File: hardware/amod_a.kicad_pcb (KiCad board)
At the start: 4 copper layers, 100 x 100 mm, 189 parts, among them J1001 SMA, J1002 SMA, J1003 SMA, J1004 SMA, J101 USB-C, J102 rails, J1101 SMA, J1102 TX, J1103 RX, J1104 Pmod, J1201 SMA, J1202 SMA, J1203 SPK, J1204 MIC, J201 SMA, J202 SMA, J301 SMA, J302 SMA, J401 SMA, J402 SMA, J501 SMA, J502 HB100, J601 SMA, J701 SMA, J702 SMA, J801 SMA, J901 SMA, J902 SMA, J903 SMA, Q1001 AO3401A, Q1101 AO3401A, Q1201 AO3401A, Q201 AO3401A, Q301 AO3401A, Q401 AO3401A, Q501 AO3401A, Q601 AO3401A, Q701 AO3401A, Q801 AO3401A, Q802 AO3400A, Q901 AO3401A, SW1001 ON, SW1002 DIP4, SW1101 ON, SW1201 ON, SW201 ON, SW301 ON, SW401 ON, SW501 ON, SW601 ON, SW701 ON, SW801 ON, SW901 ON, U1001 OPA810, U1002 OPA810, U101 LM2664, U102 3.3V, U1101 DRV8837, U1102 OPA810, U1201 PAM8302A, U1202 OPA810, U201 OPA810, U301 OPA810, U401 OPA847, U501 OPA810, U601 TLV3501, U701 74HC4046A, U801 TMP235, U901 MC1496

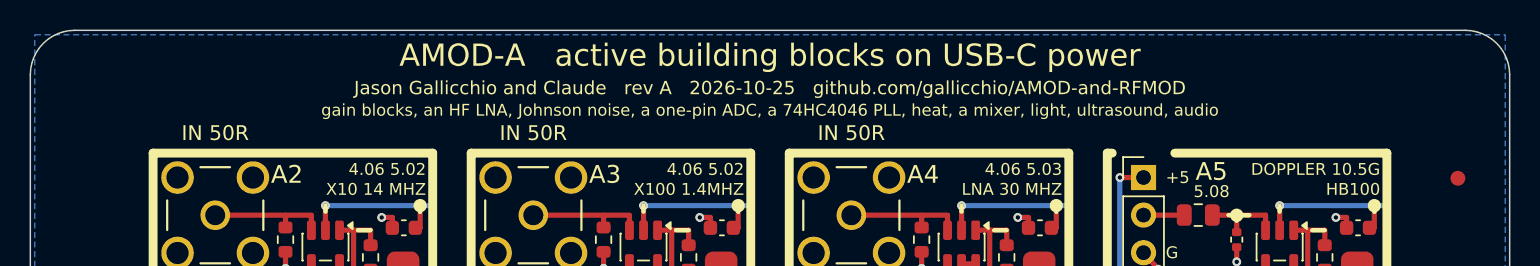
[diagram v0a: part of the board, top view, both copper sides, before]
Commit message: RF-MOD-2 rev A: the coherent I/Q transceiver board (Prompt 13)
Eleven tiles for the ECP5-2ADC-2DAC board: an ADL5375-05 modulator fed by its
DACs (X1), an ADL5380 demodulator with two OPA810 difference amplifiers into its
ADCs (X2), RF-MOD's MAX2871 synthesizer with its own REF IN (X3) split by a
resistive splitter into both LOs (X5), the QPL9547 LNA (X4), an AD8318 log
detector (X6), a switched avalanche noise source with an ADL5611 and a 20 dB
pad (X7), a GNSS front end (bias-T, SAW, MAX2659, SAW: X8), a loop for NV
centres' ODMR with every plane cleared under it (X9), USB-C and -5 V (X10) and
a SKY13370 absorptive SPDT on two Pmod lines (X11).  ERC, DRC and every fab
check pass; parts $98.61 a board.  ADL5380's 14 in stock is recorded as Jason's
accepted exception in parts.py and check_outputs reports it.

Generators: per-tile copper voids; hidden stacked symbol pins are passive (a
hidden power input made a global net of its name); schematic chips spaced by
their labels' widths and wrapped; the result note's real height sizes the
part rows; synth_tile can carry REF IN at BR1 and extra Pmod pads.

Co-Authored-By: Claude Opus 5.5 <noreply@anthropic.com>
Claude-Session: https://claude.ai/code/session_01RKeoKvFFzjk3cEBLCXXHnB
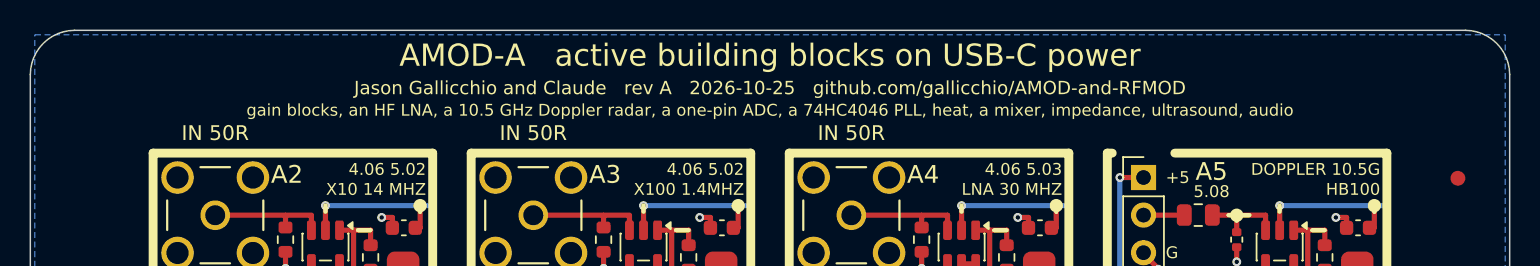
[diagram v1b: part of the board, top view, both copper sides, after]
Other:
- board text added: "gain blocks, an HF LNA, a 10.5 GHz Doppler radar, a one-pin ADC, a 74HC4046 PLL, heat, a mixer, impedance, ultrasound, audio"
- board text removed: "gain blocks, an HF LNA, Johnson noise, a one-pin ADC, a 74HC4046 PLL, heat, a mixer, light, ultrasound, audio"
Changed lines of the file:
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@@
 		)
 	)
-	(gr_text "gain blocks, an HF LNA, Johnson noise, a one-pin ADC, a 74HC4046 PLL, heat, a mixer, light, ultrasound, audio"
+	(gr_text "gain blocks, an HF LNA, a 10.5 GHz Doppler radar, a one-pin ADC, a 74HC4046 PLL, heat, a mixer, impedance, ultrasound, audio"
 		(at 50 5.4 0)
 		(layer "F.SilkS")

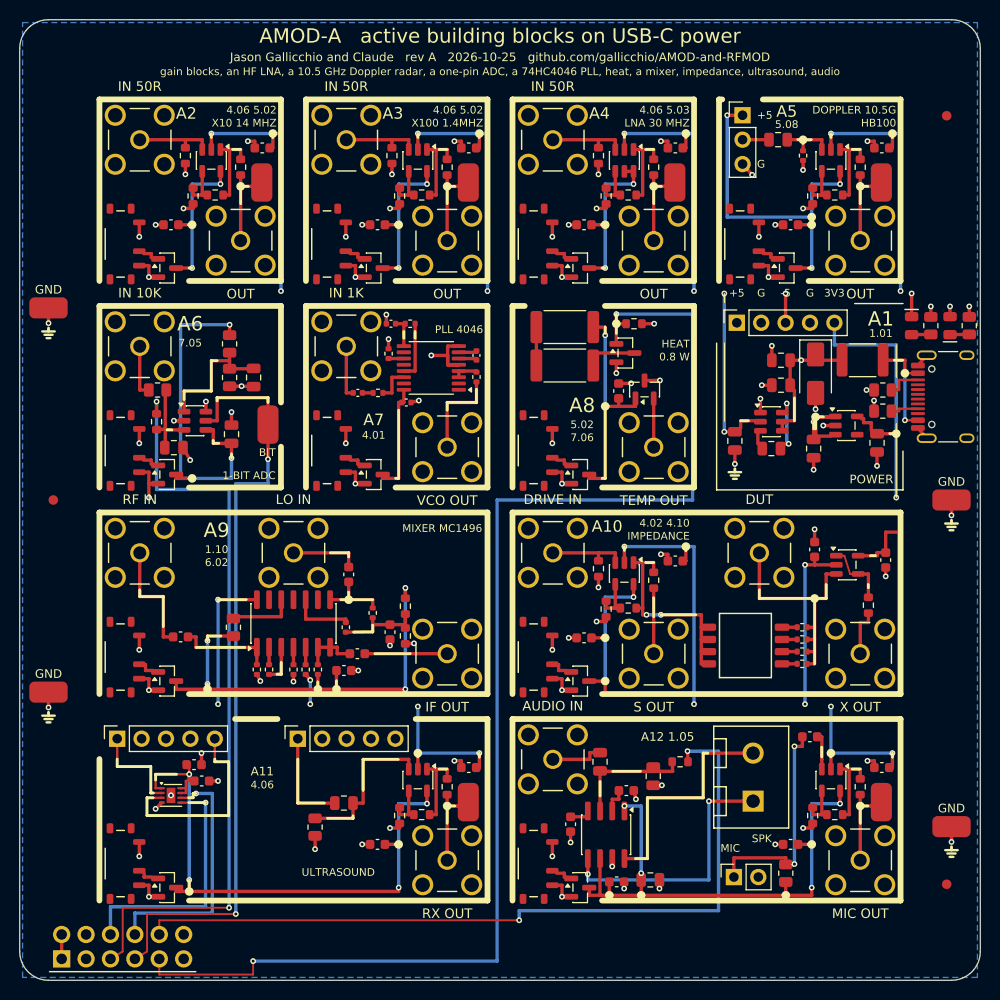
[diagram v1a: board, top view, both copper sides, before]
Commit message: Silkscreen says what each tile is and whose jack is whose: jack names on their own tile's frame, titles in words on the top frame, ranges and levels placed inside; tutorial section numbers off the boards; README tables of every tile (what, chip link, specs, limits, experiments, use, what to buy) and handbook entries as tables with a picture of each tile, both from boards/tile_docs.py
Co-Authored-By: Claude Opus 5.5 <noreply@anthropic.com>
Claude-Session: https://claude.ai/code/session_01RKeoKvFFzjk3cEBLCXXHnB
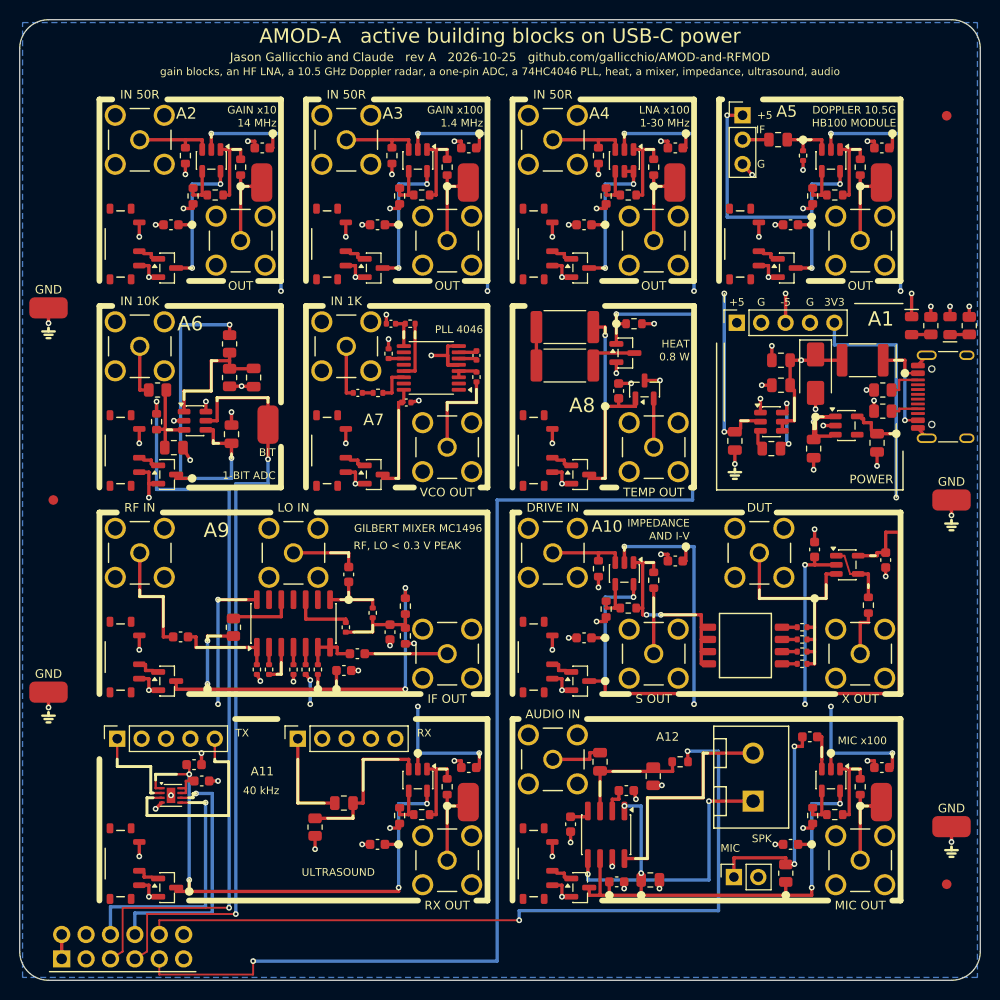
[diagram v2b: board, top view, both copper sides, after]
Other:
- board text added: "1-30 MHz"
- board text added: "1.4 MHz"
- board text added: "14 MHz"
- board text added: "40 kHz"
- board text added: "A12"
- board text added: "AND I-V"
- board text added: "GAIN x10"
- board text added: "GAIN x100"
- board text added: "GILBERT MIXER MC1496"
- board text added: "HB100 MODULE"
- board text added: "IF"
- board text added: "LNA x100"
- board text added: "MIC x100"
- board text added: "RF, LO < 0.3 V PEAK"
- board text added: "RX"
- board text added: "TX"
- board text removed: "1.01"
- board text removed: "1.10"
- board text removed: "4.01"
- board text removed: "4.02 4.10"
- board text removed: "4.06"
- board text removed: "4.06 5.02"
- board text removed: "4.06 5.03"
- board text removed: "5.02"
- board text removed: "5.08"
- board text removed: "6.02"
- board text removed: "7.05"
- board text removed: "7.06"
- board text removed: "A12 1.05"
- board text removed: "HB100"
- board text removed: "LNA 30 MHZ"
- board text removed: "MIXER MC1496"
- board text removed: "X10 14 MHZ"
- board text removed: "X100 1.4MHZ"

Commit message: A12: the speaker channel's jack is SPEAKER IN (whose input: the speaker's), beside MIC OUT; A11's docs say its 5 V powers the TX bridge and the RX op amp
Co-Authored-By: Claude Opus 5.5 <noreply@anthropic.com>
Claude-Session: https://claude.ai/code/session_01RKeoKvFFzjk3cEBLCXXHnB
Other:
- board text added: "SPEAKER IN"
- board text removed: "AUDIO IN"
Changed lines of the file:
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@@
 	)
 	(gr_line
-		(start 51.3 72.8)
-		(end 51.948572 72.8)
-		(stroke
-			(width 0.6)
-			(type default)
-		)
-		(layer "F.SilkS")
-	)
-	(gr_line
 		(start 51.3 91.7)
-		(end 51.3 72.8)
+		(end 51.3 73.24)
 		(stroke
 			(width 0.6)
@@
 	)
 	(gr_line
-		(start 59.051428 72.8)
+		(start 60.037143 72.8)
 		(end 91.7 72.8)
 		(stroke
@@
 		)
 	)
-	(gr_text "AUDIO IN"
+	(gr_text "SPEAKER IN"
 		(at 55.5 72.2976 0)
 		(layer "F.SilkS")

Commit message: Silk case convention on all six boards (Jason, Prompt 17: "To distinguish whole-tile labels from SMA or port labels, use different cases")
Ports (the jacks' names, terminal and loop names, a port named inside a note) stay UPPER CASE.  A tile's label (its
title on the frame, its name in the corner) is Mixed case: the first letter capitalised and the rest as written ("RC
low-pass", "Synthesizer", "I/Q demodulator"; tiles.label_case).  Ranges, values and notes are lower case except units,
acronyms and part numbers ("loss 1.7 dB", "OUT floats").  RF-MOD-2's X1 and X2 take word titles with their chips in
the info; RF-MOD's and RF-MOD-2's LNA tiles are titled "Preamp" ("Low-noise amp" does not fit a cell's frame); a few
two-line labels moved 0.15-0.3 mm for the descenders mixed case brings.  AMOD-P2's tile records (tile_docs), its DOA
list, KIT.md's AMOD-P2 section; X5's calibration points at P14.  All six boards: ERC 0, DRC 0, all fab checks.

Co-Authored-By: Claude Opus 5.5 <noreply@anthropic.com>
Claude-Session: https://claude.ai/code/session_01RKeoKvFFzjk3cEBLCXXHnB
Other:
- board text added: "1-bit ADC"
- board text added: "Doppler 10.5G"
- board text added: "Gilbert mixer MC1496"
- board text added: "HB100 module"
- board text added: "Heat"
- board text added: "Impedance"
- board text added: "Power"
- board text added: "RF, LO < 0.3 V peak"
- board text added: "Ultrasound"
- board text added: "and I-V"
- board text removed: "1-BIT ADC"
- board text removed: "AND I-V"
- board text removed: "DOPPLER 10.5G"
- board text removed: "GILBERT MIXER MC1496"
- board text removed: "HB100 MODULE"
- board text removed: "HEAT"
- board text removed: "IMPEDANCE"
- board text removed: "POWER"
- board text removed: "RF, LO < 0.3 V PEAK"
- board text removed: "ULTRASOUND"
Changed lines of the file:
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@@
 		)
 	)
-	(gr_text "ULTRASOUND"
+	(gr_text "Ultrasound"
 		(at 29.35 88.75 0)
 		(layer "F.SilkS")
@@
 		)
 	)
-	(gr_text "RF, LO < 0.3 V PEAK"
+	(gr_text "RF, LO < 0.3 V peak"
 		(at 34.75 54.75 0)
 		(layer "F.SilkS")
@@
 		)
 	)
-	(gr_text "1-BIT ADC"
+	(gr_text "1-bit ADC"
 		(at 26.65 47.45 0)
 		(layer "F.SilkS")
@@
 		)
 	)
-	(gr_text "GILBERT MIXER MC1496"
+	(gr_text "Gilbert mixer MC1496"
 		(at 48.15 52.95 0)
 		(layer "F.SilkS")
@@
 		)
 	)
-	(gr_text "HEAT"
+	(gr_text "Heat"
 		(at 69.75 33.75 0)
 		(layer "F.SilkS")
@@
 		)
 	)
-	(gr_text "IMPEDANCE"
+	(gr_text "Impedance"
 		(at 69.75 52.4 0)
 		(layer "F.SilkS")
@@
 		)
 	)
-	(gr_text "AND I-V"
+	(gr_text "and I-V"
 		(at 69.75 53.75 0)
 		(layer "F.SilkS")
@@
 		)
 	)
-	(gr_text "DOPPLER 10.5G"
+	(gr_text "HB100 module"
 		(at 91.25 9.4 0)
 		(layer "F.SilkS")
@@
 		)
 	)
-	(gr_text "HB100 MODULE"
+	(gr_text "Doppler 10.5G"
 		(at 91.25 10.75 0)
 		(layer "F.SilkS")
@@
 		)
 	)
-	(gr_text "POWER"
+	(gr_text "Power"
 		(at 90.95 47.85 0)
 		(layer "F.SilkS")
